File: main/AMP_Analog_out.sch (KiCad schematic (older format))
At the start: 12 parts, among them U2 TPA6110A2DGN

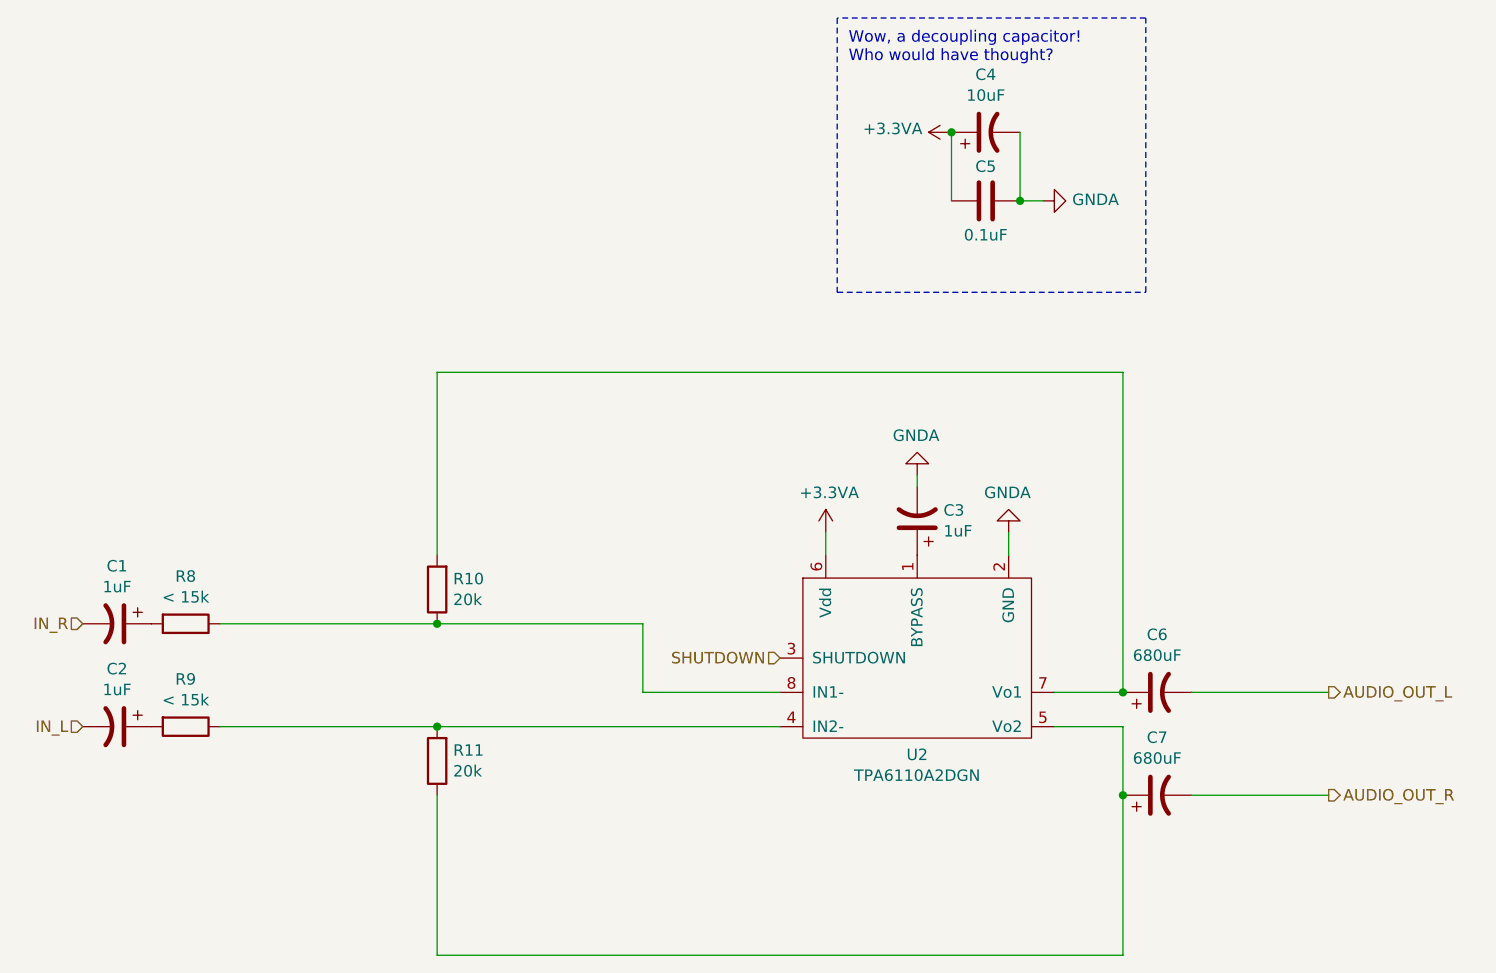
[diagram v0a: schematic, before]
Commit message: Fix up after review
Done:
- Add bulk decoupling capacitor to switch regulator cirucit
- Disconnect DONE from PROGRAM_B in FPGA (mistake)
- The decoupling capacitors used for the FPGA were for the 15T, not the
  100T. It was also setup for two I/O banks, we only use one. Disconnect
  I/O bank 15.
- Switch external clock on the MCU to an oscillator, allowing for 72MHz
- Switch pinout of the backup SPI on the MCU so that half the pins are
  ground

Mizzing:
- Add low-pass filters to the output of the DAC as per the datasheet.
  May remove the need for the amplifier circuit.
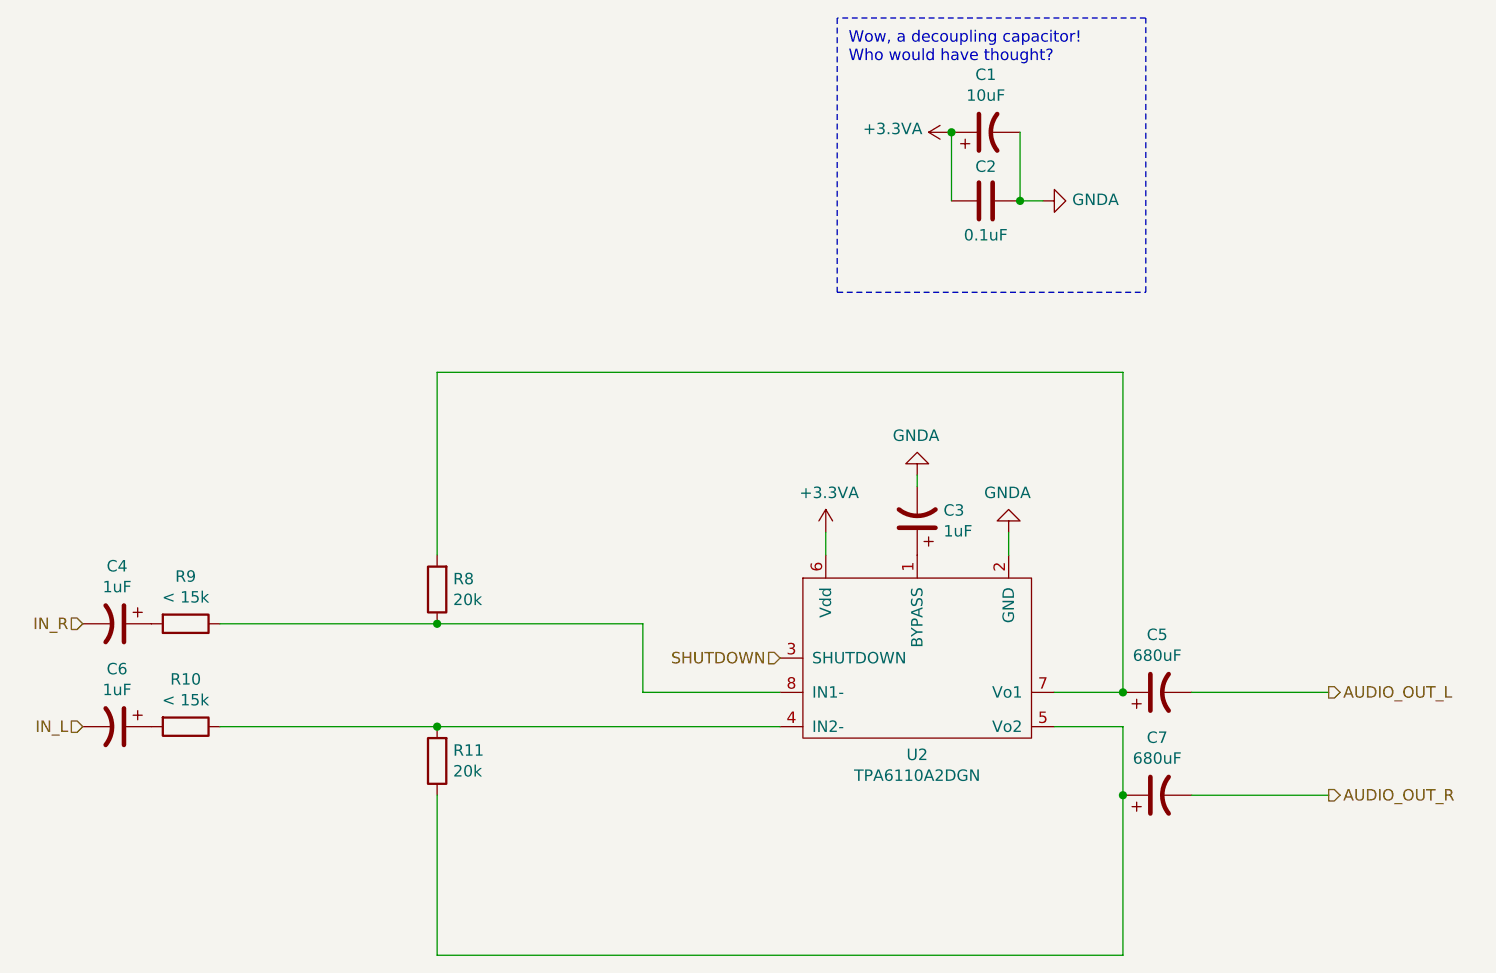
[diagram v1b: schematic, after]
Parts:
- R10: renamed from R9; footprint (none) -> Resistor_SMD:R_0805_2012Metric_Pad1.20x1.40mm_HandSolder
- R11: footprint (none) -> Resistor_SMD:R_0805_2012Metric_Pad1.20x1.40mm_HandSolder
- R8: renamed from R10; footprint (none) -> Resistor_SMD:R_0805_2012Metric_Pad1.20x1.40mm_HandSolder
- R9: renamed from R8; footprint (none) -> Resistor_SMD:R_0805_2012Metric_Pad1.20x1.40mm_HandSolder
- renumbered C4 to C1, C5 to C2, C1 to C4, C6 to C5, C2 to C6
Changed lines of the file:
@@
 SHUTDOWN
 $Comp
-L power:+3.3VA #PWR07
+L power:+3.3VA #PWR010
 U 1 1 6144EAAF
 P 5600 3300
-F 0 "#PWR07" H 5600 3150 50  0001 C CNN
+F 0 "#PWR010" H 5600 3150 50  0001 C CNN
 F 1 "+3.3VA" H 5615 3473 50  0000 C CNN
 F 2 "" H 5600 3300 50  0001 C CNN
@@
 $EndComp
 $Comp
-L power:GNDA #PWR011
+L power:GNDA #PWR08
 U 1 1 6144FB76
 P 6550 1850
-F 0 "#PWR011" H 6550 1600 50  0001 C CNN
+F 0 "#PWR08" H 6550 1600 50  0001 C CNN
 F 1 "GNDA" V 6555 1722 50  0000 R CNN
 F 2 "" H 6550 1850 50  0001 C CNN
@@
 $EndComp
 $Comp
-L power:GNDA #PWR08
+L power:GNDA #PWR09
 U 1 1 61450313
 P 6000 3050
-F 0 "#PWR08" H 6000 2800 50  0001 C CNN
+F 0 "#PWR09" H 6000 2800 50  0001 C CNN
 F 1 "GNDA" H 6005 2877 50  0000 C CNN
 F 2 "" H 6000 3050 50  0001 C CNN
@@
 $EndComp
 $Comp
-L power:+3.3VA #PWR09
+L power:+3.3VA #PWR07
 U 1 1 614535B7
 P 6150 1550
-F 0 "#PWR09" H 6150 1400 50  0001 C CNN
+F 0 "#PWR07" H 6150 1400 50  0001 C CNN
 F 1 "+3.3VA" V 6165 1677 50  0000 L CNN
 F 2 "" H 6150 1550 50  0001 C CNN
@@
 $EndComp
 $Comp
-L Device:CP1 C4
+L Device:CP1 C1
 U 1 1 61453C17
 P 6300 1550
-F 0 "C4" V 6552 1550 50  0000 C CNN
+F 0 "C1" V 6552 1550 50  0000 C CNN
 F 1 "10uF" V 6461 1550 50  0000 C CNN
 F 2 "" H 6300 1550 50  0001 C CNN
@@
 	7000 1050 5650 1050
 $Comp
-L Device:CP1 C1
+L Device:CP1 C4
 U 1 1 61459645
 P 2500 3700
-F 0 "C1" V 2248 3700 50  0000 C CNN
+F 0 "C4" V 2248 3700 50  0000 C CNN
 F 1 "1uF" V 2339 3700 50  0000 C CNN
 F 2 "" H 2500 3700 50  0001 C CNN
@@
 $EndComp
 $Comp
-L Device:CP1 C2
+L Device:CP1 C6
 U 1 1 6145AB50
 P 2500 4150
-F 0 "C2" V 2248 4150 50  0000 C CNN
+F 0 "C6" V 2248 4150 50  0000 C CNN
 F 1 "1uF" V 2339 4150 50  0000 C CNN
 F 2 "" H 2500 4150 50  0001 C CNN
@@
 $EndComp
 $Comp
-L Device:R R8
+L Device:R R9
 U 1 1 6145F753
 P 2800 3700
-F 0 "R8" V 2593 3700 50  0000 C CNN
+F 0 "R9" V 2593 3700 50  0000 C CNN
 F 1 "< 15k" V 2684 3700 50  0000 C CNN
-F 2 "" V 2730 3700 50  0001 C CNN
+F 2 "Resistor_SMD:R_0805_2012Metric_Pad1.20x1.40mm_HandSolder" V 2730 3700 50  0001 C CNN
 F 3 "~" H 2800 3700 50  0001 C CNN
 	1    2800 3700
@@
 $EndComp
 $Comp
-L Device:R R9
+L Device:R R10
 U 1 1 614603F8
 P 2800 4150
-F 0 "R9" V 2593 4150 50  0000 C CNN
+F 0 "R10" V 2593 4150 50  0000 C CNN
 F 1 "< 15k" V 2684 4150 50  0000 C CNN
-F 2 "" V 2730 4150 50  0001 C CNN
+F 2 "Resistor_SMD:R_0805_2012Metric_Pad1.20x1.40mm_HandSolder" V 2730 4150 50  0001 C CNN
 F 3 "~" H 2800 4150 50  0001 C CNN
 	1    2800 4150
@@
 	2950 4150 3900 4150
 $Comp
-L Device:R R10
+L Device:R R8
 U 1 1 6146A9F3
 P 3900 3550
-F 0 "R10" H 3830 3504 50  0000 R CNN
+F 0 "R8" H 3830 3504 50  0000 R CNN
 F 1 "20k" H 3830 3595 50  0000 R CNN
-F 2 "" V 3830 3550 50  0001 C CNN
+F 2 "Resistor_SMD:R_0805_2012Metric_Pad1.20x1.40mm_HandSolder" V 3830 3550 50  0001 C CNN
 F 3 "~" H 3900 3550 50  0001 C CNN
 	1    3900 3550
@@
 F 0 "R11" H 3830 4254 50  0000 R CNN
 F 1 "20k" H 3830 4345 50  0000 R CNN
-F 2 "" V 3830 4300 50  0001 C CNN
+F 2 "Resistor_SMD:R_0805_2012Metric_Pad1.20x1.40mm_HandSolder" V 3830 4300 50  0001 C CNN
 F 3 "~" H 3900 4300 50  0001 C CNN
 	1    3900 4300
@@
 	3900 5150 3900 4450
 $Comp
-L Device:CP1 C6
+L Device:CP1 C5
 U 1 1 6146CB5D
 P 7050 4000
-F 0 "C6" V 7302 4000 50  0000 C CNN
+F 0 "C5" V 7302 4000 50  0000 C CNN
 F 1 "680uF" V 7211 4000 50  0000 C CNN
 F 2 "" H 7050 4000 50  0001 C CNN
@@
 	6900 4450 6900 5150
 $Comp
-L Device:C C5
+L Device:C C2
 U 1 1 6146271B
 P 6300 1850
-F 0 "C5" V 6150 1850 50  0000 C CNN
+F 0 "C2" V 6150 1850 50  0000 C CNN
 F 1 "0.1uF" V 6450 1850 50  0000 C CNN
 F 2 "" H 6338 1700 50  0001 C CNN
@@
 	6400 3300 6400 3400
 $Comp
-L power:GNDA #PWR010
+L power:GNDA #PWR011
 U 1 1 616EC208
 P 6400 3300
-F 0 "#PWR010" H 6400 3050 50  0001 C CNN
+F 0 "#PWR011" H 6400 3050 50  0001 C CNN
 F 1 "GNDA" H 6405 3127 50  0000 C CNN
 F 2 "" H 6400 3300 50  0001 C CNN

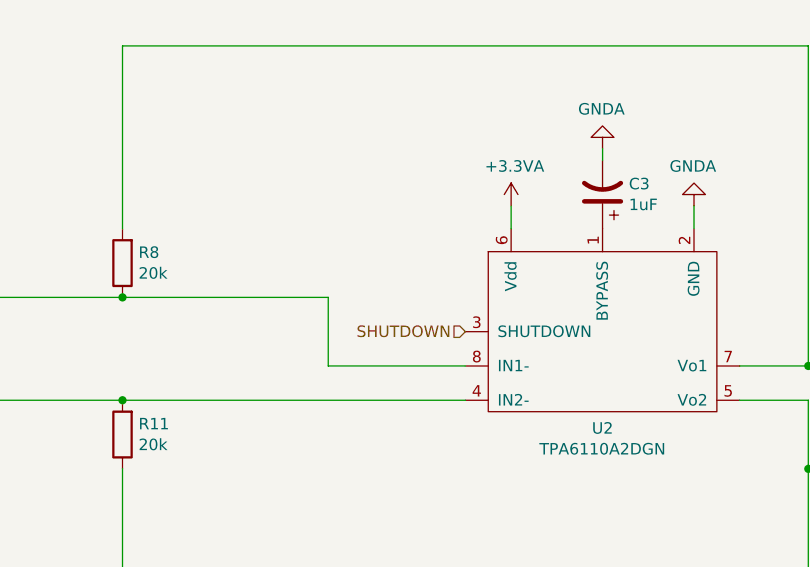
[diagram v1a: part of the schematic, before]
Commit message: Fix up after review 2
Don't route DAC_ZERO_{L,R} through FPGA into SHUTDOWN on the amp, it is
not really necessary and just adds routing complexity.
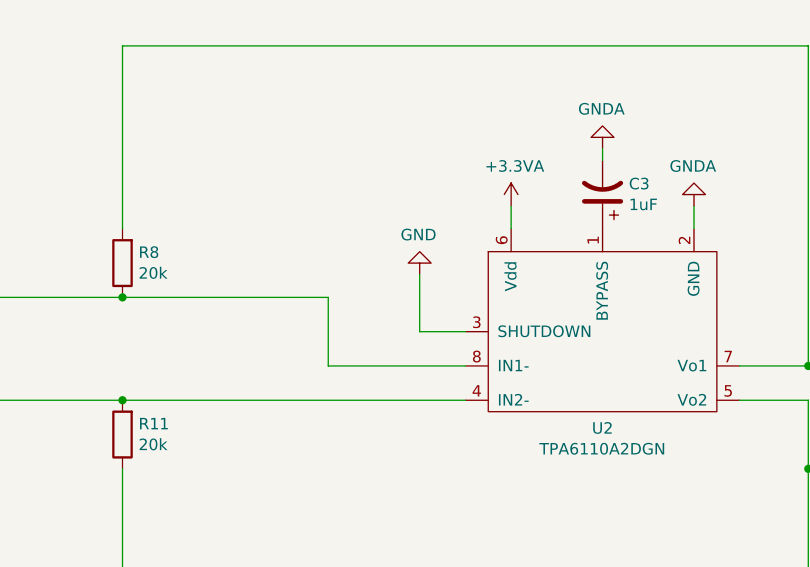
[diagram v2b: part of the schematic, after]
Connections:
- net SHUTDOWN renamed GND
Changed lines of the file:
@@
 Text HLabel 2350 3700 0    50   Input ~ 0
 IN_R
-Text HLabel 5400 3850 0    50   Input ~ 0
-SHUTDOWN
 $Comp
 L power:+3.3VA #PWR010
@@
 	-1   0    0    1
 $EndComp
+$Comp
+L power:GND #PWR?
+U 1 1 61C66B7F
+P 5200 3600
+F 0 "#PWR?" H 5200 3350 50  0001 C CNN
+F 1 "GND" H 5205 3427 50  0000 C CNN
+F 2 "" H 5200 3600 50  0001 C CNN
+F 3 "" H 5200 3600 50  0001 C CNN
+	1    5200 3600
+	-1   0    0    1
+$EndComp
+Wire Wire Line
+	5200 3600 5200 3850
+Wire Wire Line
+	5200 3850 5400 3850
 $EndSCHEMATC

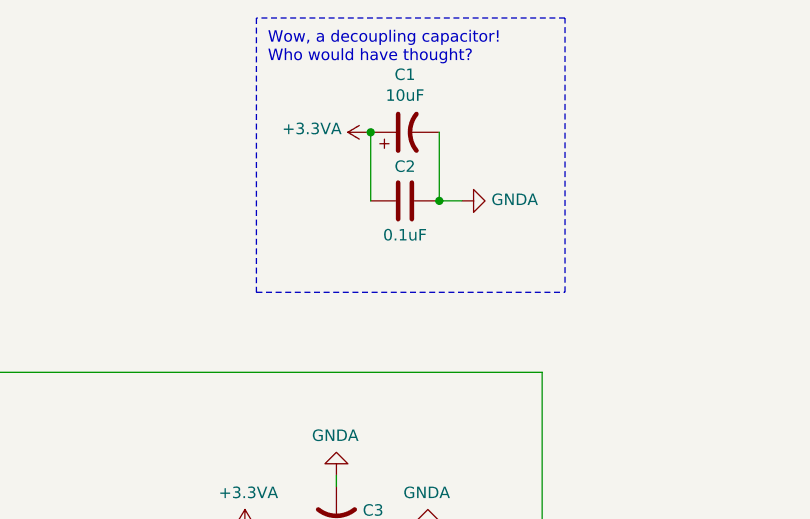
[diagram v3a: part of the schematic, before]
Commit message: DAC: Remove amplifier, replace with low pass as per datasheet
Also: a lot of footprint association
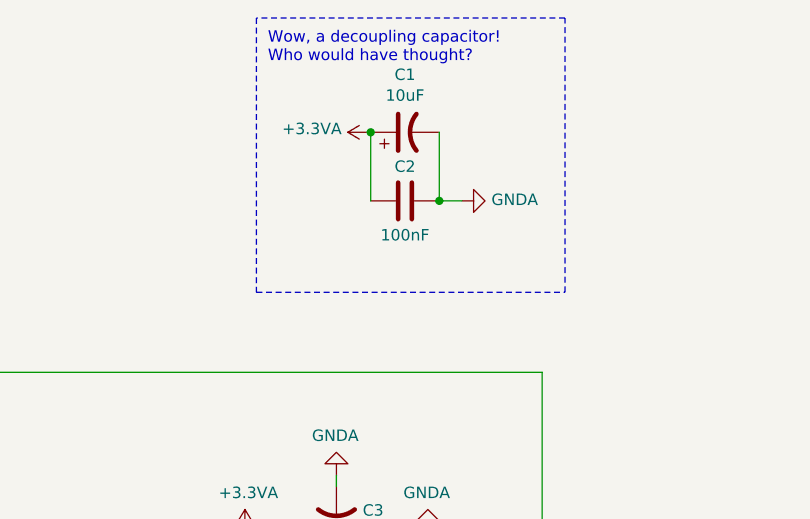
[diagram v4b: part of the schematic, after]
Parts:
- C2: value 0.1uF -> 100nF; footprint (none) -> Capacitor_SMD:C_0805_2012Metric_Pad1.18x1.45mm_HandSolder
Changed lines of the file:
@@
 P 6300 1850
 F 0 "C2" V 6150 1850 50  0000 C CNN
-F 1 "0.1uF" V 6450 1850 50  0000 C CNN
-F 2 "" H 6338 1700 50  0001 C CNN
+F 1 "100nF" V 6450 1850 50  0000 C CNN
+F 2 "Capacitor_SMD:C_0805_2012Metric_Pad1.18x1.45mm_HandSolder" H 6338 1700 50  0001 C CNN
 F 3 "~" H 6300 1850 50  0001 C CNN
 	1    6300 1850
